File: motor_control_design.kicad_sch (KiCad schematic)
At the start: 87 parts, among them J1 TYPE-C-31-M-12, J10 3V3, J2 SWD, J3 VBAT, J4 GND, J5 FC_M/P, J6 Conn_01x06, J8 Conn_01x06, J9 GND, Q1 RF1S9540SM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

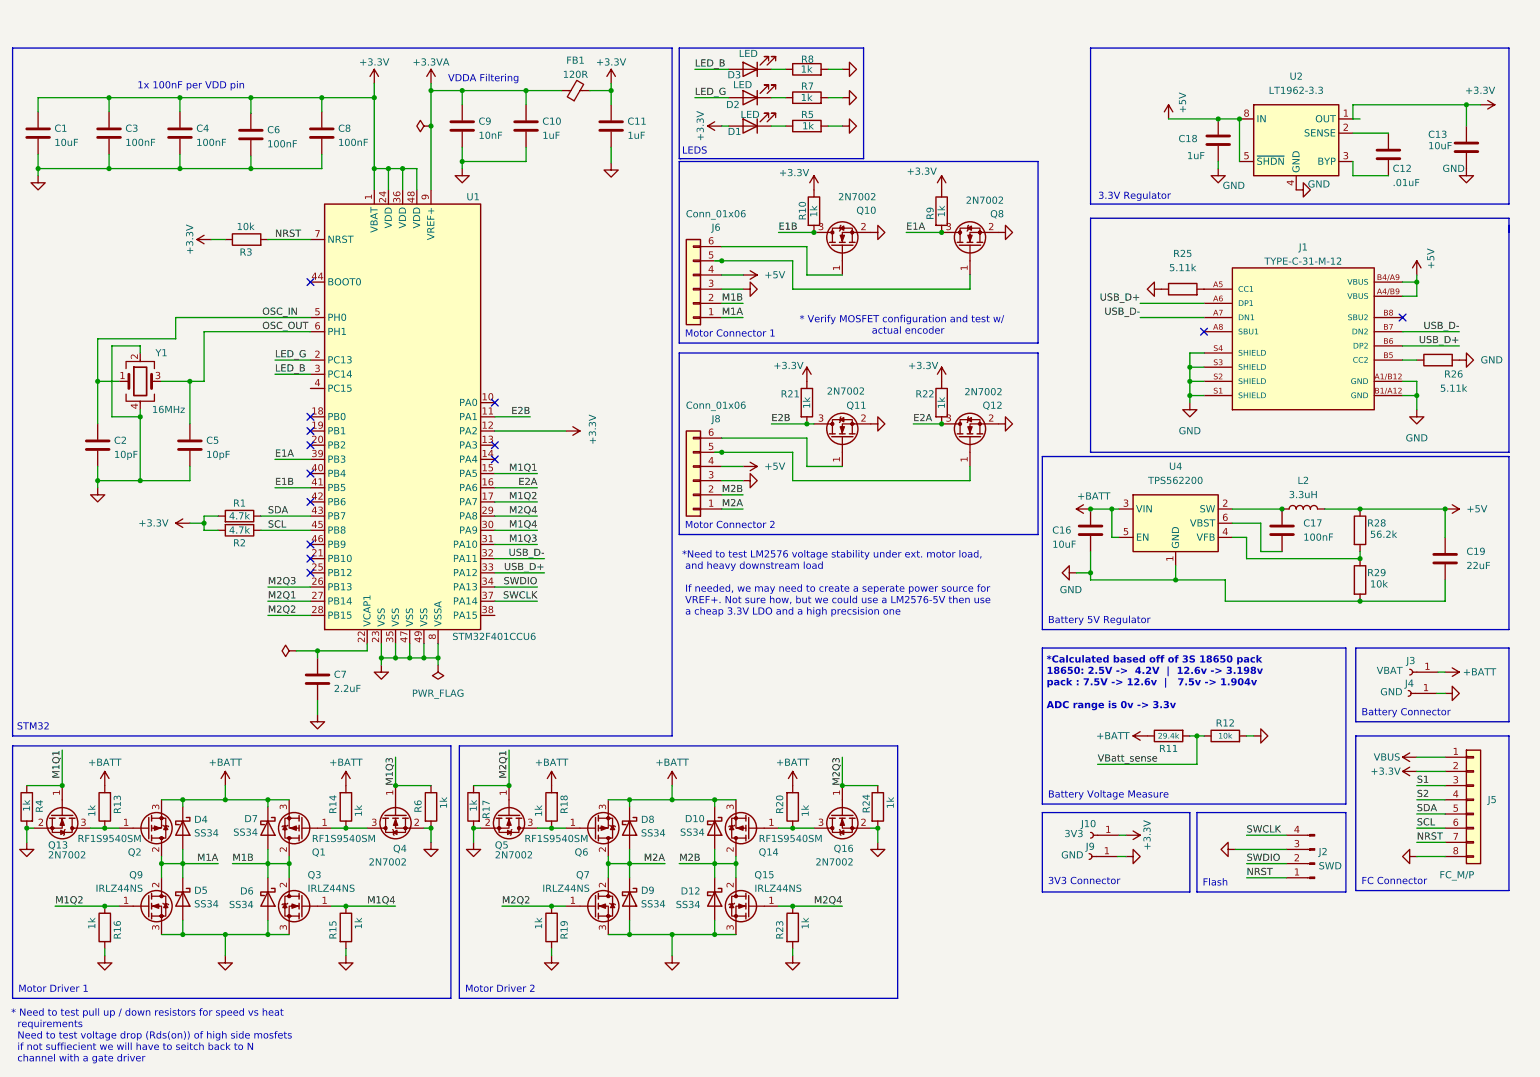
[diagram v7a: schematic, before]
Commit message: added i2c, moved batt and ground pads back from edge
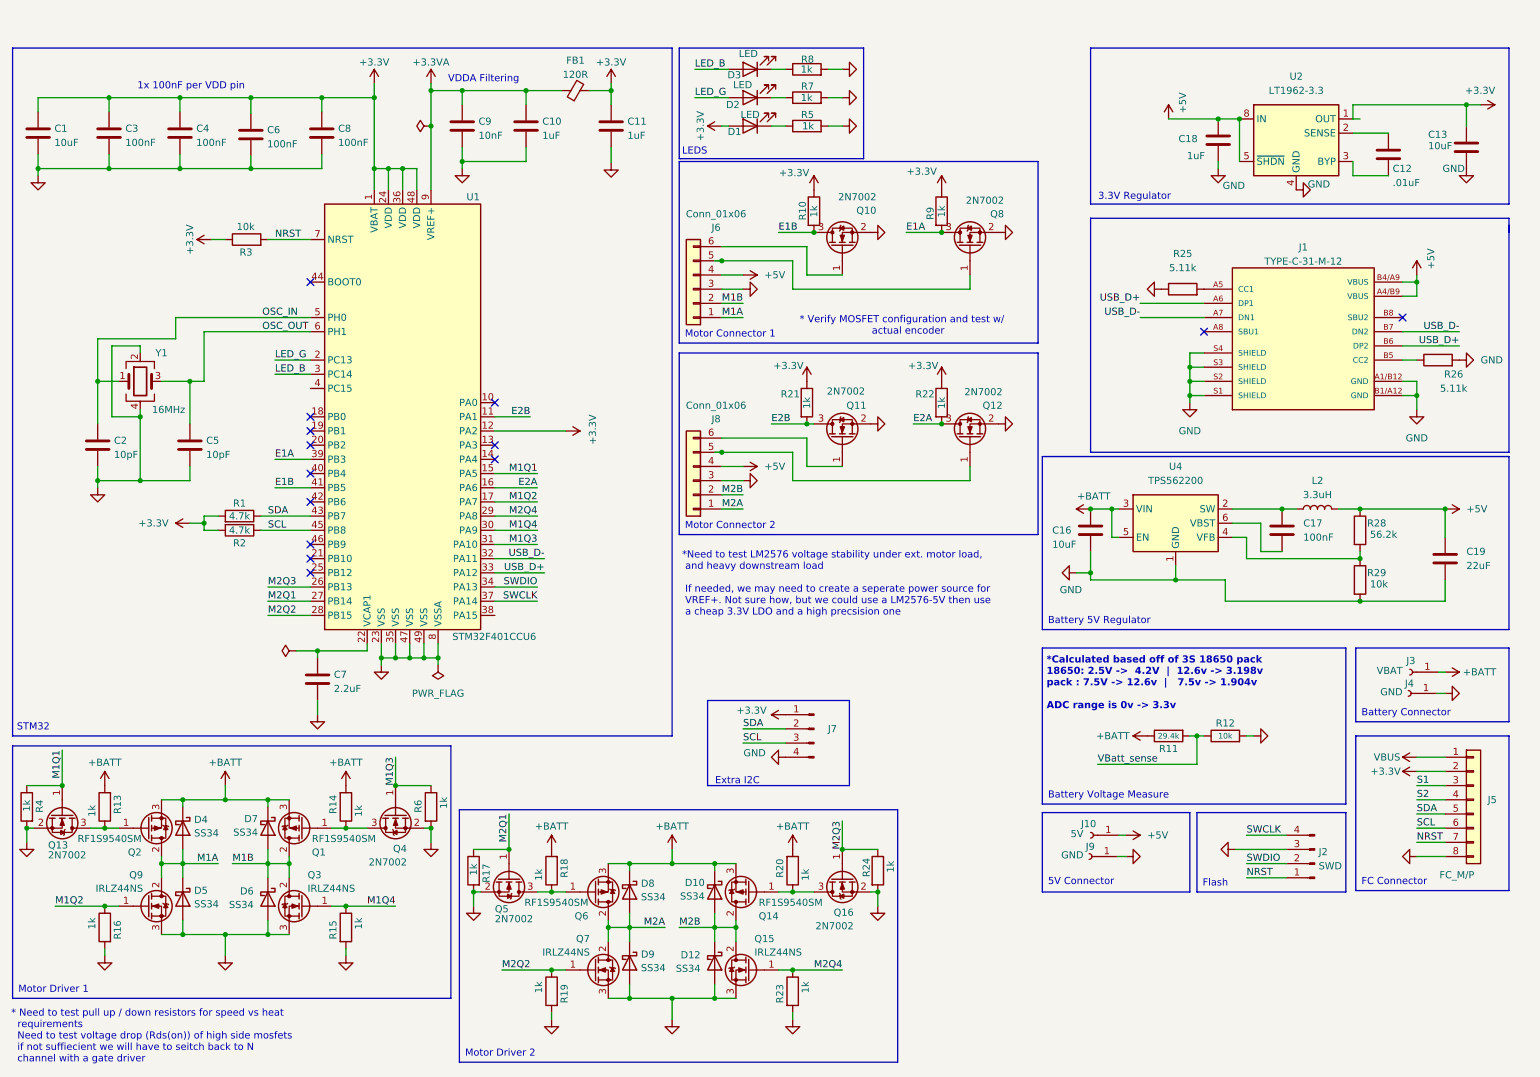
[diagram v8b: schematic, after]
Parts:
- added J7: Conn_01x04_Pin, Connector_JST:JST_SH_BM04B-SRSS-TB_1x04-1MP_P1.00mm_Vertical, symbol Connector:Conn_01x04_Pin
- J10: value 3V3 -> 5V
- J6, J8: footprint JST-XH-SMD:CONN_S6B-XH-SM4-TB_JST -> Custom:CONN_S6B-XH-SM4-TB_JST
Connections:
- net +3.3V: now also J7.1 (Pin_1); no longer J10.1 (Pin_1)
- net +5V: now also J10.1 (Pin_1)
- net GND: now also J7.4 (Pin_4)
- net SCL: now also J7.3 (Pin_3)
- net SDA: now also J7.2 (Pin_2)
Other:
- note added: "5V Connector"
- note added: "Extra I2C"
- note removed: "3V3 Connector"
- moved on the sheet: D10, D12, D8, D9, L2, Q14, Q15, Q16, Q5, Q6, Q7, R17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
